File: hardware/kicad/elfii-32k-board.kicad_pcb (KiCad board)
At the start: 2 copper layers, 177.8 x 127.1 mm, 15 parts, among them J1 ELFII_86_MECH_UNVERIFIED, U1 74HCT273, U2 62256, U3 74HCT04, U4 74HCT86, U5 74HCT32

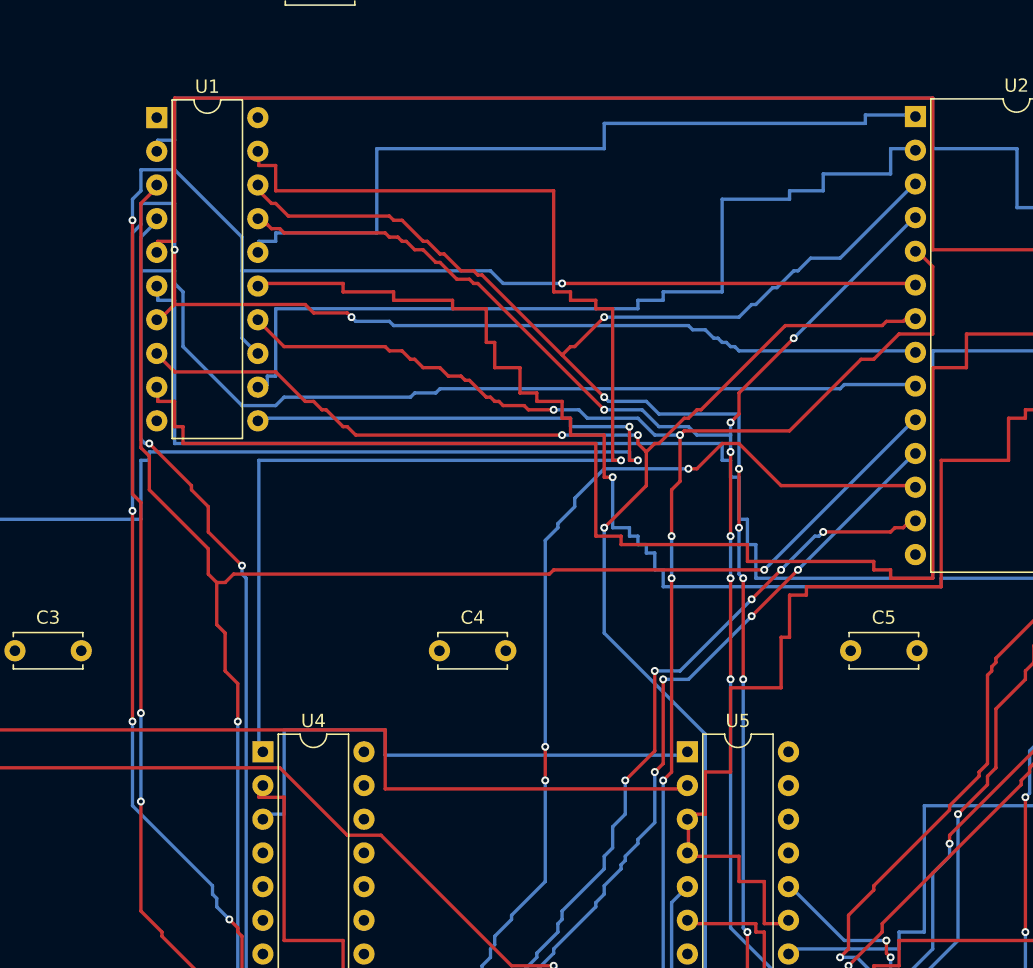
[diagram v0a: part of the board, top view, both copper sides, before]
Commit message: Explicitly bridge all isolated GND and +5V plane islands in full-route candidate
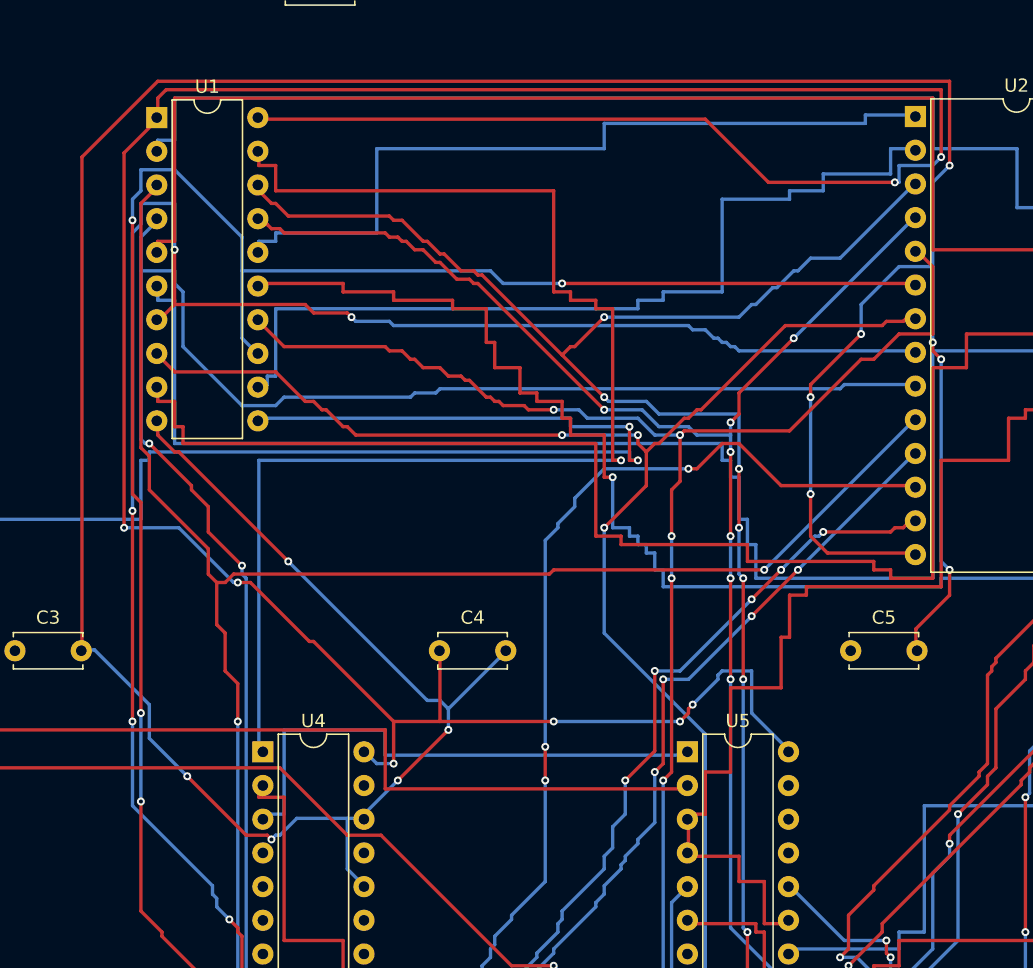
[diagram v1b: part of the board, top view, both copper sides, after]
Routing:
- net /GND: track 6.50 -> 274.7 mm, vias 1 -> 13
- net /VCC: track 6.50 -> 233.5 mm, vias 1 -> 9

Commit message: Link all 14 verified component instances to project-local ELFII_32K footprint library
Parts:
- C1, C2, C3, C4, C5: footprint Capacitor_THT:C_Disc_D5.0mm_W2.5mm_P5.00mm -> ELFII_32K:C_Disc_D5.0mm_W2.5mm_P5.00mm
- JP1: footprint Connector_PinHeader_2.54mm:PinHeader_1x03_P2.54mm_Vertical -> ELFII_32K:PinHeader_1x03_P2.54mm_Vertical
- JP2: footprint Connector_PinHeader_2.54mm:PinHeader_1x02_P2.54mm_Vertical -> ELFII_32K:PinHeader_1x02_P2.54mm_Vertical
- R1, R2: footprint Resistor_THT:R_Axial_DIN0207_L6.3mm_D2.5mm_P7.62mm_Horizontal -> ELFII_32K:R_Axial_DIN0207_L6.3mm_D2.5mm_P7.62mm_Horizontal
- U1: footprint Package_DIP:DIP-20_W7.62mm -> ELFII_32K:DIP-20_W7.62mm
- U2: footprint Package_DIP:DIP-28_W15.24mm -> ELFII_32K:DIP-28_W15.24mm
- U3, U4, U5: footprint Package_DIP:DIP-14_W7.62mm -> ELFII_32K:DIP-14_W7.62mm
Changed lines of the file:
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@@
   (pad "1" smd rect (at 106.6800 0) (size 1.397 8.890) (layers "B.Cu" "B.Mask") (net 37 "/VCC") (zone_connect 2))
 )
-(footprint "Package_DIP:DIP-20_W7.62mm" (layer "F.Cu") (at 88.19 55.57)
+(footprint "ELFII_32K:DIP-20_W7.62mm" (layer "F.Cu") (at 88.19 55.57)
   (attr through_hole)
   (descr "20-lead though-hole mounted DIP package, row spacing 7.62 mm (300 mils)")
@@
 )
 )
-(footprint "Package_DIP:DIP-28_W15.24mm" (layer "F.Cu") (at 145.38 55.49)
+(footprint "ELFII_32K:DIP-28_W15.24mm" (layer "F.Cu") (at 145.38 55.49)
   (attr through_hole)
   (descr "28-lead though-hole mounted DIP package, row spacing 15.24 mm (600 mils)")
@@
 )
 )
-(footprint "Package_DIP:DIP-14_W7.62mm" (layer "F.Cu") (at 64.19 103.38)
+(footprint "ELFII_32K:DIP-14_W7.62mm" (layer "F.Cu") (at 64.19 103.38)
   (attr through_hole)
   (descr "14-lead though-hole mounted DIP package, row spacing 7.62 mm (300 mils)")
@@
 )
 )
-(footprint "Package_DIP:DIP-14_W7.62mm" (layer "F.Cu") (at 96.19 103.38)
+(footprint "ELFII_32K:DIP-14_W7.62mm" (layer "F.Cu") (at 96.19 103.38)
   (attr through_hole)
   (descr "14-lead though-hole mounted DIP package, row spacing 7.62 mm (300 mils)")
@@
 )
 )
-(footprint "Package_DIP:DIP-14_W7.62mm" (layer "F.Cu") (at 128.19 103.38)
+(footprint "ELFII_32K:DIP-14_W7.62mm" (layer "F.Cu") (at 128.19 103.38)
   (attr through_hole)
   (descr "14-lead though-hole mounted DIP package, row spacing 7.62 mm (300 mils)")
@@
 )
 )
-(footprint "Connector_PinHeader_2.54mm:PinHeader_1x03_P2.54mm_Vertical" (layer "F.Cu") (at 190 80)
+(footprint "ELFII_32K:PinHeader_1x03_P2.54mm_Vertical" (layer "F.Cu") (at 190 80)
   (attr through_hole)
   (descr "Through hole straight pin header, 1x03, 2.54mm pitch, single row")
@@
 )
 )
-(footprint "Connector_PinHeader_2.54mm:PinHeader_1x02_P2.54mm_Vertical" (layer "F.Cu") (at 190 107)
+(footprint "ELFII_32K:PinHeader_1x02_P2.54mm_Vertical" (layer "F.Cu") (at 190 107)
   (attr through_hole)
   (descr "Through hole straight pin header, 1x02, 2.54mm pitch, single row")
@@
 )
 )
-(footprint "Resistor_THT:R_Axial_DIN0207_L6.3mm_D2.5mm_P7.62mm_Horizontal" (layer "F.Cu") (at 172.19 123)
+(footprint "ELFII_32K:R_Axial_DIN0207_L6.3mm_D2.5mm_P7.62mm_Horizontal" (layer "F.Cu") (at 172.19 123)
   (attr through_hole)
   (descr "Resistor, Axial_DIN0207 series, Axial, Horizontal, pin pitch=7.62mm, 0.25W = 1/4W, length*diameter=6.3*2.5mm^2, http://cdn-reichelt.de/documents/datenblatt/B400/1_4W%23YAG.pdf")
@@
 )
 )
-(footprint "Resistor_THT:R_Axial_DIN0207_L6.3mm_D2.5mm_P7.62mm_Horizontal" (layer "F.Cu") (at 172.19 132)
+(footprint "ELFII_32K:R_Axial_DIN0207_L6.3mm_D2.5mm_P7.62mm_Horizontal" (layer "F.Cu") (at 172.19 132)
   (attr through_hole)
   (descr "Resistor, Axial_DIN0207 series, Axial, Horizontal, pin pitch=7.62mm, 0.25W = 1/4W, length*diameter=6.3*2.5mm^2, http://cdn-reichelt.de/documents/datenblatt/B400/1_4W%23YAG.pdf")
@@
 )
 )
-(footprint "Capacitor_THT:C_Disc_D5.0mm_W2.5mm_P5.00mm" (layer "F.Cu") (at 98 45.72)
+(footprint "ELFII_32K:C_Disc_D5.0mm_W2.5mm_P5.00mm" (layer "F.Cu") (at 98 45.72)
   (attr through_hole)
   (descr "C, Disc series, Radial, pin pitch=5.00mm, , diameter*width=5*2.5mm^2, Capacitor, http://cdn-reichelt.de/documents/datenblatt/B300/DS_KERKO_TC.pdf")
@@
 )
 )
-(footprint "Capacitor_THT:C_Disc_D5.0mm_W2.5mm_P5.00mm" (layer "F.Cu") (at 166.5 47)
+(footprint "ELFII_32K:C_Disc_D5.0mm_W2.5mm_P5.00mm" (layer "F.Cu") (at 166.5 47)
   (attr through_hole)
   (descr "C, Disc series, Radial, pin pitch=5.00mm, , diameter*width=5*2.5mm^2, Capacitor, http://cdn-reichelt.de/documents/datenblatt/B300/DS_KERKO_TC.pdf")
@@
 )
 )
-(footprint "Capacitor_THT:C_Disc_D5.0mm_W2.5mm_P5.00mm" (layer "F.Cu") (at 77.5 95.76)
+(footprint "ELFII_32K:C_Disc_D5.0mm_W2.5mm_P5.00mm" (layer "F.Cu") (at 77.5 95.76)
   (attr through_hole)
   (descr "C, Disc series, Radial, pin pitch=5.00mm, , diameter*width=5*2.5mm^2, Capacitor, http://cdn-reichelt.de/documents/datenblatt/B300/DS_KERKO_TC.pdf")
@@
 )
 )
-(footprint "Capacitor_THT:C_Disc_D5.0mm_W2.5mm_P5.00mm" (layer "F.Cu") (at 109.5 95.76)
+(footprint "ELFII_32K:C_Disc_D5.0mm_W2.5mm_P5.00mm" (layer "F.Cu") (at 109.5 95.76)
   (attr through_hole)
   (descr "C, Disc series, Radial, pin pitch=5.00mm, , diameter*width=5*2.5mm^2, Capacitor, http://cdn-reichelt.de/documents/datenblatt/B300/DS_KERKO_TC.pdf")
@@
 )
 )
-(footprint "Capacitor_THT:C_Disc_D5.0mm_W2.5mm_P5.00mm" (layer "F.Cu") (at 140.5 95.76)
+(footprint "ELFII_32K:C_Disc_D5.0mm_W2.5mm_P5.00mm" (layer "F.Cu") (at 140.5 95.76)
   (attr through_hole)
   (descr "C, Disc series, Radial, pin pitch=5.00mm, , diameter*width=5*2.5mm^2, Capacitor, http://cdn-reichelt.de/documents/datenblatt/B300/DS_KERKO_TC.pdf")

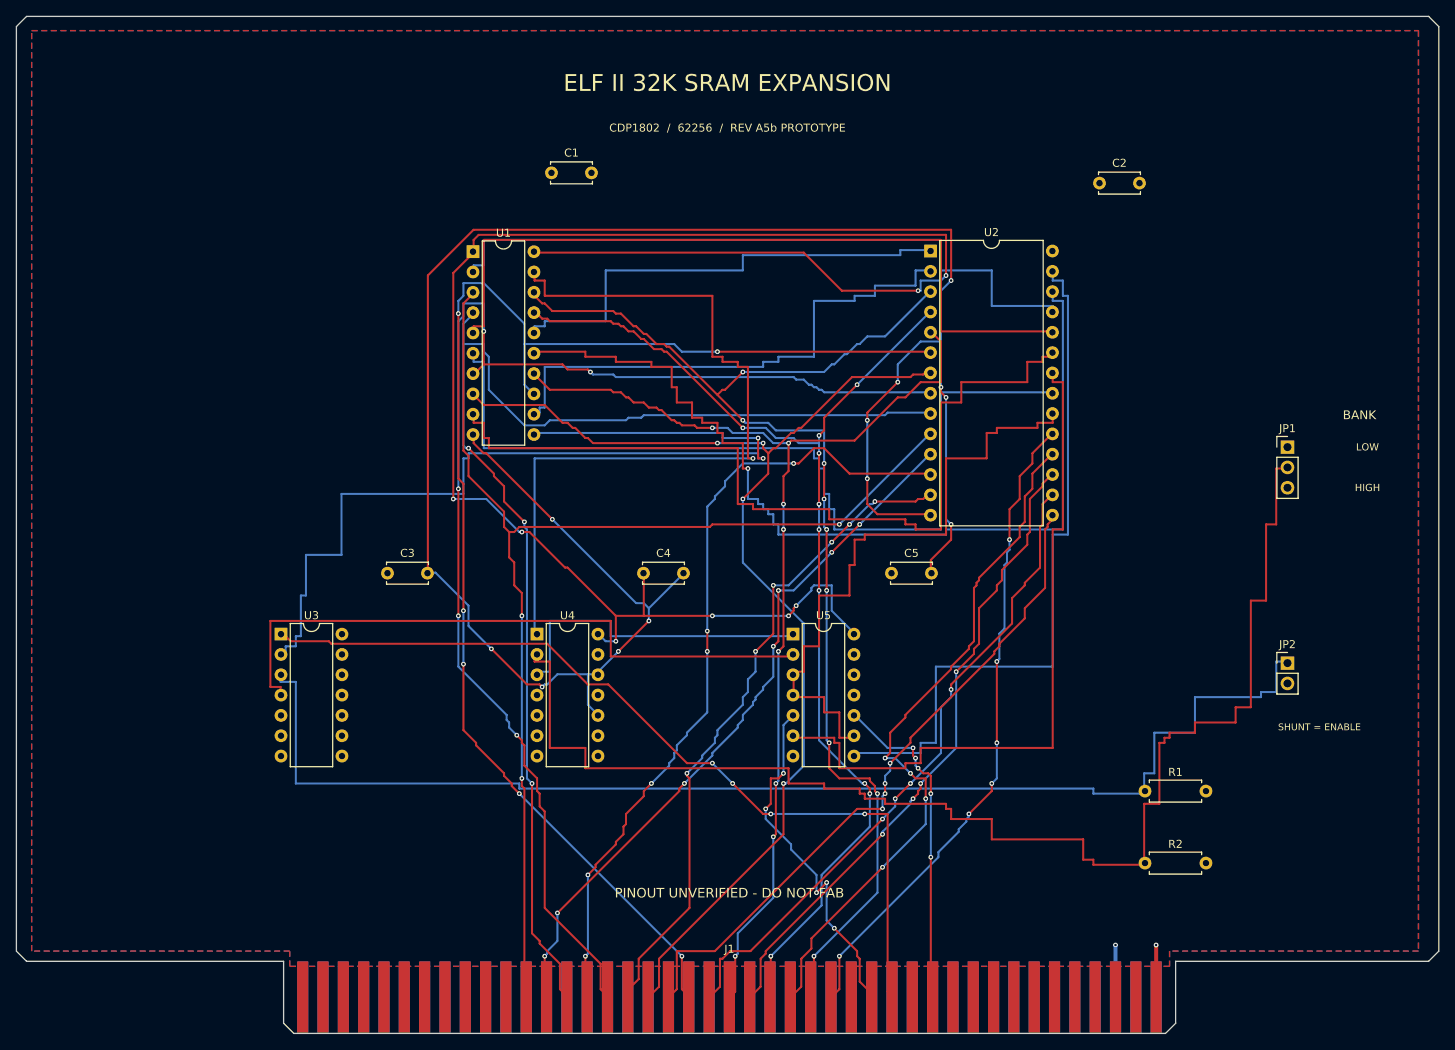
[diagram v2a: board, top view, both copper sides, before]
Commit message: WIP: Hyperboard-derived fully connected routing preview (not for fab)
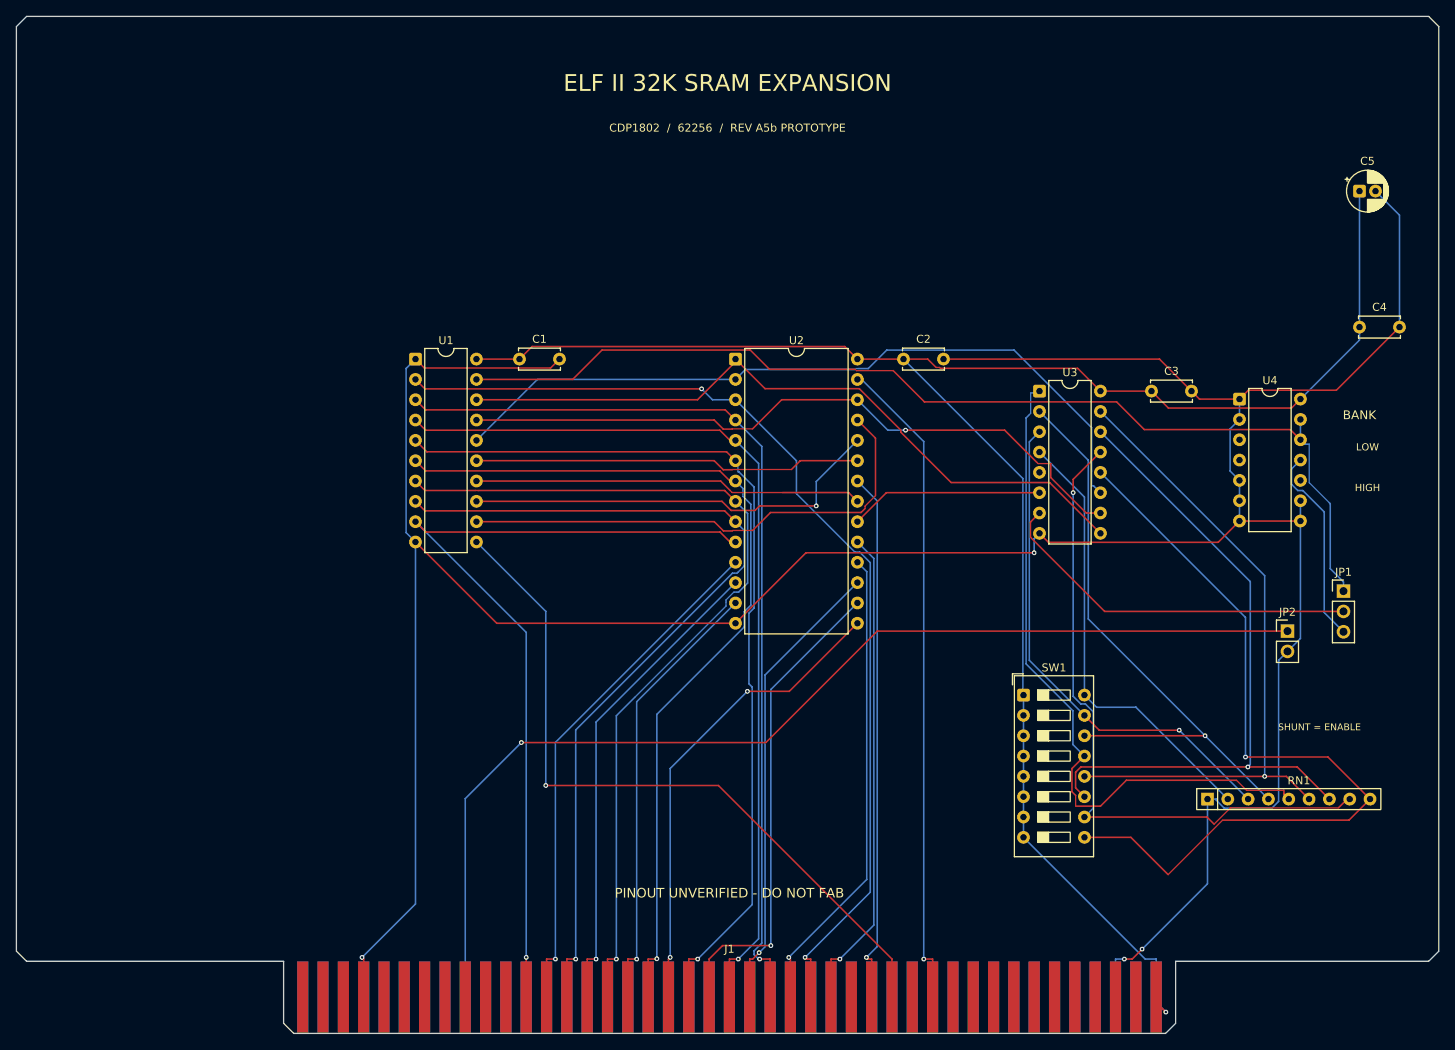
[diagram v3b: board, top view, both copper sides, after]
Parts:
- removed R1, R2: 10k, ELFII_32K:R_Axial_DIN0207_L6.3mm_D2.5mm_P7.62mm_Horizontal
- removed U5: 74HCT32, ELFII_32K:DIP-14_W7.62mm
- added RN1: 8x22K, R_Array_SIP9, F.Cu at (180.0, 124.0)
- added SW1: RAM_PAGE_ENABLE, SW_DIP_SPSTx08_Slide_9.78x22.5mm_W7.62mm_P2.54mm, F.Cu at (157.0, 111.0)
- C1, C2, C3, C4: footprint ELFII_32K:C_Disc_D5.0mm_W2.5mm_P5.00mm -> C_Disc_D5.0mm_W2.5mm_P5.00mm
- C5: value 100n -> 10u POLARIZED PIN1=+5V; footprint ELFII_32K:C_Disc_D5.0mm_W2.5mm_P5.00mm -> CP_Radial_D5.0mm_P2.00mm
- JP1: value REGION_SELECT -> RAM_HALF; footprint ELFII_32K:PinHeader_1x03_P2.54mm_Vertical -> PinHeader_1x03_P2.54mm_Vertical
- JP2: value CARD_ENABLE -> MB_RAM_DISABLE_SLOT5; footprint ELFII_32K:PinHeader_1x02_P2.54mm_Vertical -> PinHeader_1x02_P2.54mm_Vertical
- U1: value 74HCT273 -> 74HC573; footprint ELFII_32K:DIP-20_W7.62mm -> DIP-20_W7.62mm
- U2: value 62256 -> CY62256-70PC; footprint ELFII_32K:DIP-28_W15.24mm -> DIP-28_W15.24mm
- U3: value 74HCT04 -> 74HC151; footprint ELFII_32K:DIP-14_W7.62mm -> DIP-16_W7.62mm
- U4: value 74HCT86 -> CD4011; footprint ELFII_32K:DIP-14_W7.62mm -> DIP-14_W7.62mm
- moved U3 99.6 mm to (159.0, 73.0)
- moved C3 98.2 mm to (173.0, 73.0)
- moved C4 94.6 mm to (199.0, 65.0)
- moved U4 92.6 mm to (184.0, 74.0)
- moved C5 75.5 mm to (199.0, 48.0)
- moved C2 32.9 mm to (142.0, 69.0)
- moved U2 27.9 mm to (121.0, 69.0)
- moved C1 23.6 mm to (94.0, 69.0)
- moved JP1 19.3 mm to (197.0, 98.0)
- moved U1 15.2 mm to (81.0, 69.0)
- moved JP2 4.00 mm to (190.0, 103.0)
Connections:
- C1 pad 1: /VCC -> +5V
- C1 pad 2: /GND -> GND
- C2 pad 1: /VCC -> +5V
- C2 pad 2: /GND -> GND
- C3 pad 1: /VCC -> +5V
- C3 pad 2: /GND -> GND
- C4 pad 1: /VCC -> +5V
- C4 pad 2: /GND -> GND
- C5 pad 1: /VCC -> +5V
- C5 pad 2: /GND -> GND
- J1 pad 1: /VCC -> +5V
- J1 pad 2: /VCC -> +5V
- J1 pad 24: /NMWR -> /~MWR
- J1 pad 30: /NMRD -> /~MRD
- J1 pad 5: /GND -> GND
- J1 pad 69: (no net) -> /MB_RAM_DISABLE
- J1 pad 80: /GND -> GND
- JP1 pad 1: /GND -> /A15
- JP1 pad 2: /REGION -> /HALF_EN
- JP1 pad 3: /VCC -> /A15_N
- JP2 pad 1: /ENABLE -> /MB_RAM_DISABLE
- JP2 pad 2: /VCC -> GND
- U1 pad 1: /VCC -> GND
- U1 pad 10: /GND -> GND
- U1 pad 11: /LATCH_CLK -> /TPA
- U1 pad 12: /A12 -> /A8
- U1 pad 13: /MA4 -> /A9
- U1 pad 14: /MA5 -> /A10
- U1 pad 15: /A13 -> /A11
- U1 pad 16: /A14 -> /A12
- U1 pad 17: /MA6 -> /A13
- U1 pad 18: /MA7 -> /A14
- U1 pad 2: /A8 -> /MA7
- U1 pad 20: /VCC -> +5V
- U1 pad 3: /MA0 -> /MA6
- U1 pad 4: /MA1 -> /MA5
- U1 pad 5: /A9 -> /MA4
- U1 pad 6: /A10 -> /MA3
- U1 pad 8: /MA3 -> /MA1
- U1 pad 9: /A11 -> /MA0
- U2 pad 14: /GND -> GND
- U2 pad 20: /NCE -> /RAM_CS_N
- U2 pad 22: /NOE -> /~MRD
- U2 pad 27: /NWE -> /~MWR
- U2 pad 28: /VCC -> +5V
- U3 pad 1: /TPA -> /PAGE3
- U3 pad 10: (no net) -> /A13
- U3 pad 11: /GND -> /A12
- U3 pad 12: (no net) -> /PAGE7
- U3 pad 13: /GND -> /PAGE6
- U3 pad 14: /VCC -> /PAGE5
- U3 pad 2: /LATCH_CLK -> /PAGE2
- U3 pad 3: /ENABLE -> /PAGE1
- U3 pad 4: /NOT_ENABLE -> /PAGE0
- U3 pad 5: /GND -> (no net)
- U3 pad 6: (no net) -> /RAM_CS_N
- U3 pad 7: /GND -> /HALF_EN
- U3 pad 8: (no net) -> GND
- U3 pad 9: /GND -> /A14
- U4 pad 1: /A15 -> GND
- U4 pad 10: /GND -> (no net)
- U4 pad 11: (no net) -> /A15_N
- U4 pad 12: /GND -> /A15
- U4 pad 13: /GND -> /A15
- U4 pad 14: /VCC -> +5V
- U4 pad 2: /REGION -> GND
- U4 pad 3: /MISMATCH -> (no net)
- U4 pad 4: /GND -> (no net)
- U4 pad 5: /GND -> GND
- U4 pad 6: (no net) -> GND
- U4 pad 7: /GND -> GND
- U4 pad 8: (no net) -> GND
- U4 pad 9: /GND -> GND
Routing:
- net GND: track 0.00 -> 401.1 mm, vias 0 -> 4
- net /GND: track 274.7 -> 0.00 mm, vias 13 -> 0
- net +5V: track 0.00 -> 234.7 mm, vias 0 -> 1
- net /VCC: track 233.5 -> 0.00 mm, vias 9 -> 0
- net /REGION: track 170.0 -> 0.00 mm
- net /ENABLE: track 157.4 -> 0.00 mm
- net /MB_RAM_DISABLE: track 0.00 -> 136.3 mm, vias 0 -> 1
- net /LATCH_CLK: track 118.4 -> 0.00 mm, vias 2 -> 0
- net /PAGE7: track 0.00 -> 102.4 mm, vias 0 -> 1
- net /NWE: track 89.8 -> 0.00 mm
- net /NOE: track 88.5 -> 0.00 mm
- net /PAGE5: track 0.00 -> 87.0 mm, vias 0 -> 1
- net /PAGE3: track 0.00 -> 86.2 mm
- net /PAGE6: track 0.00 -> 83.7 mm, vias 0 -> 1
- net /PAGE4: track 0.00 -> 83.4 mm, vias 0 -> 1
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- removed copper zone on F.Cu, net /GND
- removed copper zone on B.Cu, net /VCC
